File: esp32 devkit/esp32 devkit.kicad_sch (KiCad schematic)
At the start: 38 parts, among them J1 Conn_01x19, J2 Conn_01x19, Q1 SS8050, Q2 SS8050, SW1 SW_Push, SW2 SW_Push, U1 AMS1117-3.3, U2 ESP32-WROOM-32E(4MB), U3 CP2102N-A02-GQFN28

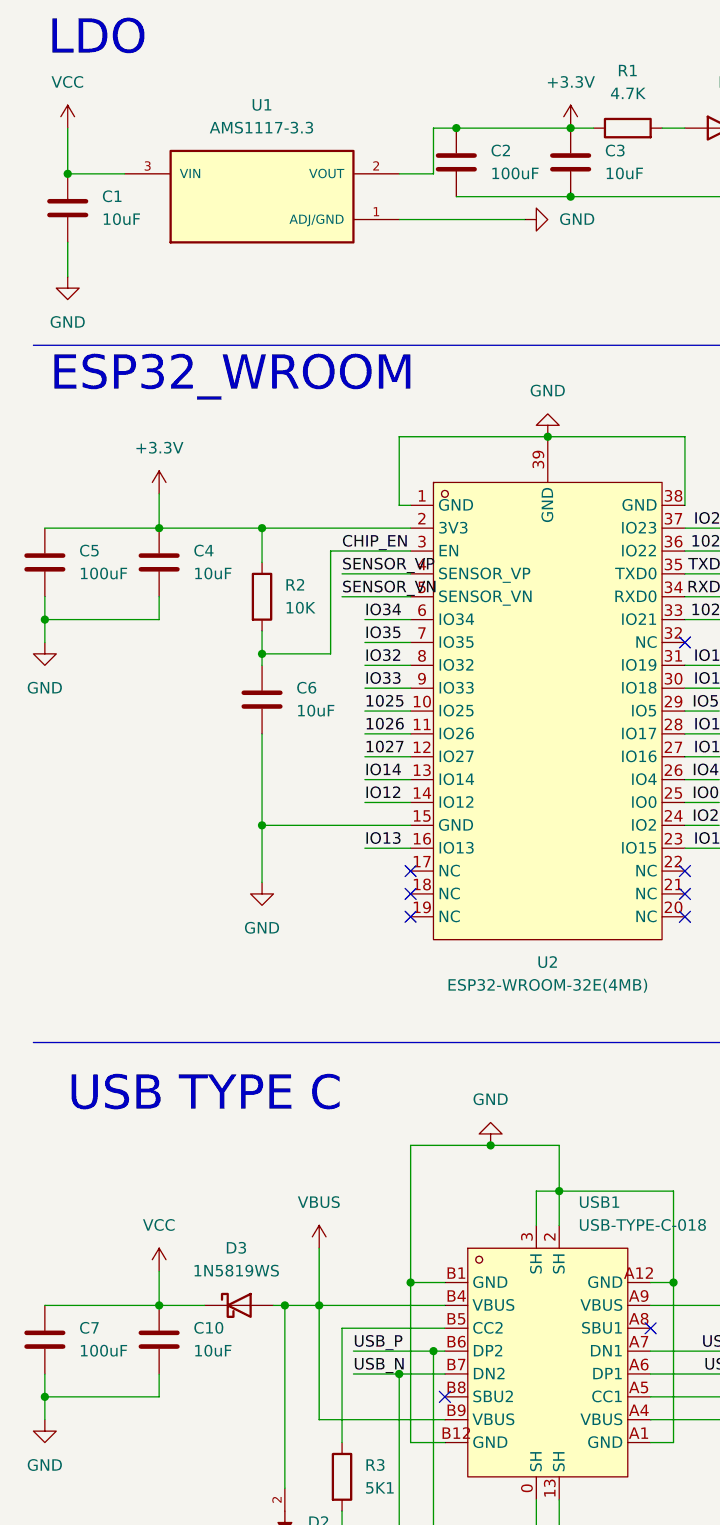
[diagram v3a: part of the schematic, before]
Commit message: :bug:Fixed errors of footprint,, started on Editor
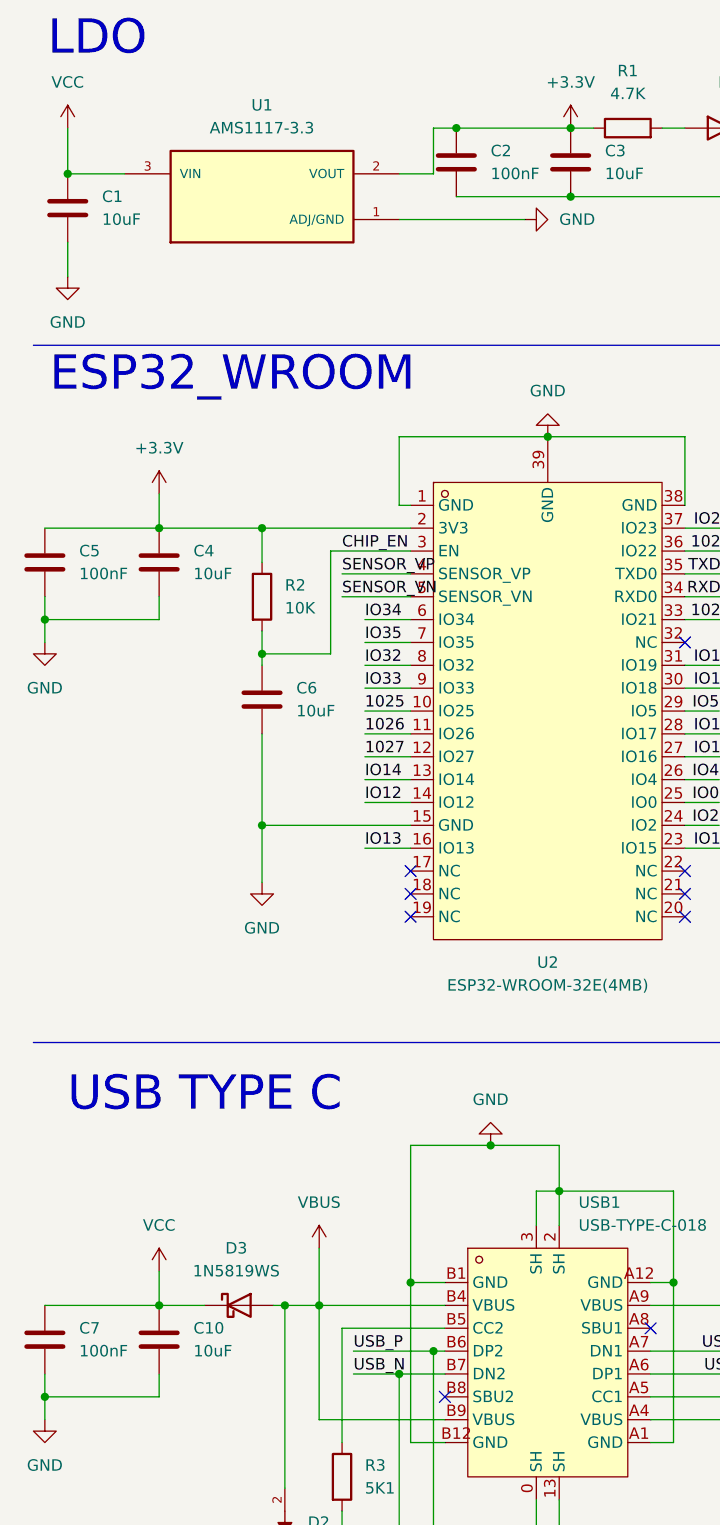
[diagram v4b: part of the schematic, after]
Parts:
- C1, C10, C3, C4, C6, C9: footprint (none) -> Capacitor_SMD:C_0603_1608Metric
- C11, C12, C8: footprint (none) -> Capacitor_SMD:C_0402_1005Metric
- C2, C5, C7: value 100uF -> 100nF; footprint (none) -> Capacitor_SMD:C_0402_1005Metric
- D1: footprint (none) -> LED_SMD:LED_0402_1005Metric
- J1, J2: footprint (none) -> Connector_PinHeader_2.54mm:PinHeader_1x19_P2.54mm_Vertical
- R1, R10, R11, R2, R3, R4, R5, R6, R7, R8, R9: footprint (none) -> Resistor_SMD:R_0402_1005Metric
- SW1, SW2: footprint (none) -> Button_Switch_SMD:SW_SPST_TL3305A
- U1: footprint AMS1117-3.3:SOT229P700X180-4N -> Package_TO_SOT_SMD:SOT-223-3_TabPin2

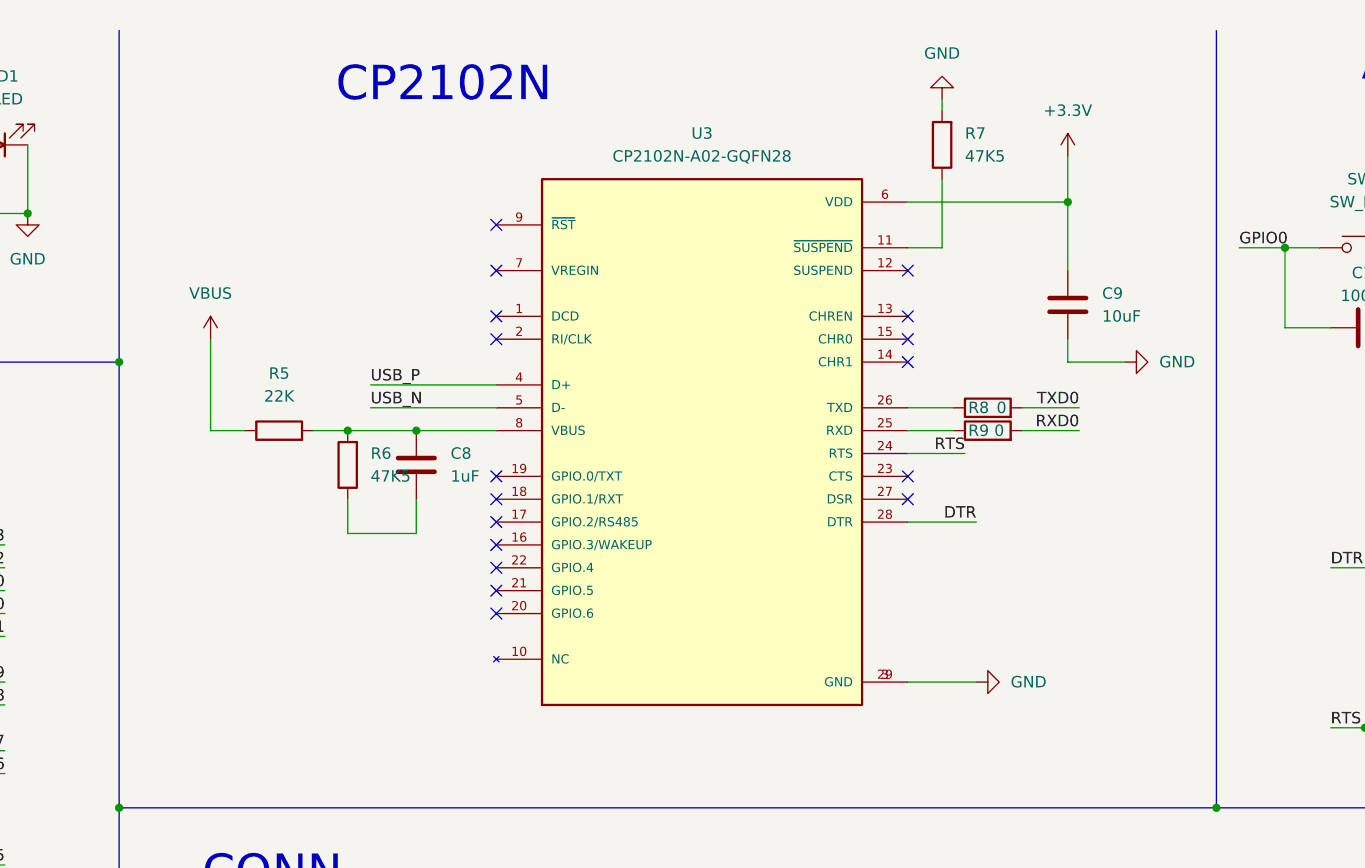
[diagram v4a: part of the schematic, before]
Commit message: :bug:changed CP2102 footprint and schematic
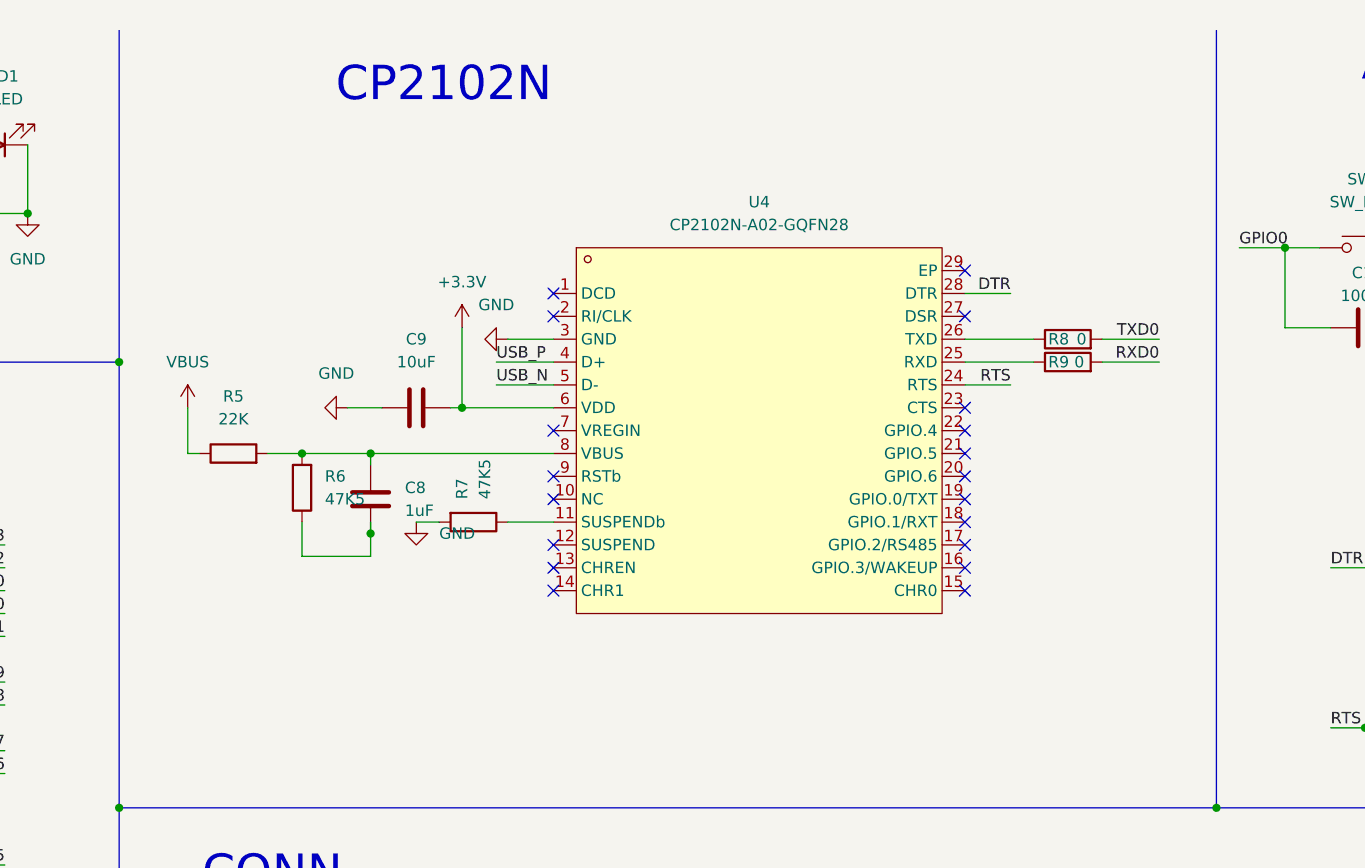
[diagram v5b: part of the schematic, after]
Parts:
- removed U3: CP2102N-A02-GQFN28, CP2102N-A02-GQFN28:QFN50P500X500X80-29N, symbol CP2102N-A02-GQFN28:CP2102N-A02-GQFN28
- added U4: CP2102N-A02-GQFN28, CP2102N-A02-GQFN28:QFN-28_L5.0-W5.0-P0.50-TL-EP3.3, symbol CP2102N-A02-GQFN28:CP2102N-A02-GQFN28
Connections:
- net +3.3V: now also C9.2, U4.6 (VDD); no longer C9.1
- net DTR: now also U4.28 (DTR)
- net GND: now also C9.1, U4.3 (GND); no longer C9.2
- net RTS: now also U4.24 (RTS)
- net USB_N: now also U4.5 (D-)
- net USB_P: now also U4.4 (D+)
- net at C8.1, R5.2, R6.2: now also U4.8 (VBUS)
- net at R7.1: now also U4.11 (SUSPENDb)
- net at R9.1: now also U4.25 (RXD)
- net at R8.1: now also U4.26 (TXD)
- no-connect marks 32 -> 34
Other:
- moved on the sheet: C8, C9, R5, R6, R7, R8, R9
